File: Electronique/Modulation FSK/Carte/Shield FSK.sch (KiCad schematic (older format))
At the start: 13 parts, among them P1 CONN_1, U1 XR2206

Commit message: Et on reroute, on reroute, on reroute, on reroute, on reroute, on reroute, on reroute, on reroute, on reroute, on reroute, on reroute, on reroute, on reroute, on reroute, on reroute, on reroute, on reroute, on reroute, on reroute, on reroute, on reroute, on reroute, on reroute, on reroute, on reroute, on reroute, on reroute, on reroute, on reroute, on reroute, on reroute, on reroute, on reroute, on reroute, on reroute, on reroute, on reroute, on reroute, on reroute, on reroute, on reroute, on reroute, on reroute, on reroute. C'est fini !!!
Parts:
- removed C1, C4: CP, symbol CP
- removed P1: CONN_1, symbol CONN_1
- added C1, C4: C, symbol C
- added P1: BNC, symbol BNC
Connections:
- net GND: now also C1.2, C4.1, P1.2 (Ext)
- net at U1.10 (BIAS): now also C4.2
- net at U1.2 (STO): now also P1.1 (In)
- net at R1.2, R2.1, RV1.2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: now also C1.1
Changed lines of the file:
@@
-EESchema Schematic File Version 2  date 23/03/2012 16:19:35
+EESchema Schematic File Version 2  date 24/03/2012 16:53:15
 LIBS:power
 LIBS:device
@@
 LIBS:contrib
 LIBS:valves
-LIBS:Arduino
-LIBS:arduino_shieldsNCL
 LIBS:Shield FSK-cache
 EELAYER 25  0
@@
 Sheet 1 1
 Title ""
-Date "23 mar 2012"
+Date "24 mar 2012"
 Rev ""
 Comp ""
@@
 Comment4 ""
 $EndDescr
-$Comp
-L CONN_1 P1
-U 1 1 4F6C926A
+Wire Wire Line
+	6400 3000 6500 3000
+Wire Wire Line
+	4400 2100 4500 2100
+Wire Wire Line
+	2850 4200 2850 4000
+Wire Wire Line
+	2600 4550 2600 4650
+Wire Wire Line
+	2600 3650 2600 4050
+Connection ~ 2600 3850
+Wire Wire Line
+	3100 3850 3100 3700
+Wire Wire Line
+	3100 3700 4600 3700
+Wire Wire Line
+	6300 3800 6400 3800
+Wire Wire Line
+	6650 4000 6450 4000
+Wire Wire Line
+	6450 4000 6450 4100
+Wire Wire Line
+	6450 4100 6300 4100
+Connection ~ 3450 4350
+Wire Wire Line
+	3600 4350 3450 4350
+Wire Wire Line
+	4100 4350 4550 4350
+Wire Wire Line
+	4550 4350 4550 4200
+Wire Wire Line
+	4550 4200 4600 4200
+Wire Wire Line
+	4100 4150 4550 4150
+Wire Wire Line
+	4550 4150 4550 4100
+Wire Wire Line
+	4550 4100 4600 4100
+Wire Wire Line
+	4600 4000 4550 4000
+Wire Wire Line
+	4200 3850 4450 3850
+Connection ~ 4450 3800
+Wire Wire Line
+	4450 3850 4450 3800
+Wire Wire Line
+	6450 3900 6300 3900
+Wire Wire Line
+	4400 3800 4600 3800
+Wire Wire Line
+	4600 3500 4350 3500
+Wire Wire Line
+	3400 3600 4600 3600
+Wire Wire Line
+	3800 3850 3700 3850
+Wire Wire Line
+	4600 3900 4150 3900
+Wire Wire Line
+	4150 3900 4150 4000
+Wire Wire Line
+	3600 4150 3450 4150
+Wire Wire Line
+	3450 4150 3450 4500
+Wire Wire Line
+	6600 4200 6300 4200
+Wire Wire Line
+	7050 4000 7200 4000
+Wire Wire Line
+	6900 3800 6900 3700
+Wire Wire Line
+	6900 3700 6300 3700
+Wire Wire Line
+	2850 4000 2600 4000
+Connection ~ 2600 4000
+Wire Wire Line
+	2600 3050 2600 3150
+Wire Wire Line
+	2850 4600 2600 4600
+Connection ~ 2600 4600
+Wire Wire Line
+	4500 2200 4400 2200
+Wire Wire Line
+	3250 3300 3250 3400
+$Comp
+L GND #PWR3
+U 1 1 4F6DEC1B
+P 3250 3300
+F 0 "#PWR3" H 3250 3300 30  0001 C CNN
+F 1 "GND" H 3250 3230 30  0001 C CNN
+	1    3250 3300
+	-1   0    0    1
+$EndComp
+$Comp
+L BNC P1
+U 1 1 4F6DEBDE
 P 3250 3600
-F 0 "P1" H 3330 3600 40  0000 L CNN
-F 1 "CONN_1" H 3250 3655 30  0001 C CNN
+F 0 "P1" H 3260 3720 60  0000 C CNN
+F 1 "BNC" V 3360 3540 40  0000 C CNN
 	1    3250 3600
 	-1   0    0    1
 $EndComp
+$Comp
+L C C4
+U 1 1 4F6DEA2A
+P 6850 4000
+F 0 "C4" H 6900 4100 50  0000 L CNN
+F 1 "C" H 6900 3900 50  0000 L CNN
+	1    6850 4000
+	0    1    1    0
+$EndComp
+$Comp
+L C C1
+U 1 1 4F6DEA20
+P 2850 4400
+F 0 "C1" H 2900 4500 50  0000 L CNN
+F 1 "C" H 2900 4300 50  0000 L CNN
+	1    2850 4400
+	1    0    0    -1
+$EndComp
 Text Label 6500 3000 0    60   ~ 0
 Entree serie
-Wire Wire Line
-	6400 3000 6500 3000
-Wire Wire Line
-	4400 2100 4500 2100
-Wire Wire Line
-	2850 4200 2850 4000
-Wire Wire Line
-	2600 4550 2600 4650
-Wire Wire Line
-	2600 3650 2600 4050
-Connection ~ 2600 3850
-Wire Wire Line
-	3100 3850 3100 3700
-Wire Wire Line
-	3100 3700 4600 3700
-Wire Wire Line
-	6300 3800 6400 3800
-Wire Wire Line
-	6650 4000 6450 4000
-Wire Wire Line
-	6450 4000 6450 4100
-Wire Wire Line
-	6450 4100 6300 4100
-Connection ~ 3450 4350
-Wire Wire Line
-	3600 4350 3450 4350
-Wire Wire Line
-	4100 4350 4550 4350
-Wire Wire Line
-	4550 4350 4550 4200
-Wire Wire Line
-	4550 4200 4600 4200
-Wire Wire Line
-	4100 4150 4550 4150
-Wire Wire Line
-	4550 4150 4550 4100
-Wire Wire Line
-	4550 4100 4600 4100
-Wire Wire Line
-	4600 4000 4550 4000
-Wire Wire Line
-	4200 3850 4450 3850
-Connection ~ 4450 3800
-Wire Wire Line
-	4450 3850 4450 3800
-Wire Wire Line
-	6450 3900 6300 3900
-Wire Wire Line
-	4400 3800 4600 3800
-Wire Wire Line
-	4600 3500 4350 3500
-Wire Wire Line
-	3400 3600 4600 3600
-Wire Wire Line
-	3800 3850 3700 3850
-Wire Wire Line
-	4600 3900 4150 3900
-Wire Wire Line
-	4150 3900 4150 4000
-Wire Wire Line
-	3600 4150 3450 4150
-Wire Wire Line
-	3450 4150 3450 4500
-Wire Wire Line
-	6600 4200 6300 4200
-Wire Wire Line
-	7050 4000 7200 4000
-Wire Wire Line
-	6900 3800 6900 3700
-Wire Wire Line
-	6900 3700 6300 3700
-Wire Wire Line
-	2850 4000 2600 4000
-Connection ~ 2600 4000
-Wire Wire Line
-	2600 3050 2600 3150
-Wire Wire Line
-	2850 4600 2600 4600
-Connection ~ 2600 4600
-Wire Wire Line
-	4500 2200 4400 2200
-$Comp
-L GND #PWR7
+$Comp
+L GND #PWR8
 U 1 1 4F6B897D
 P 4400 2200
-F 0 "#PWR7" H 4400 2200 30  0001 C CNN
+F 0 "#PWR8" H 4400 2200 30  0001 C CNN
 F 1 "GND" H 4400 2130 30  0001 C CNN
 	1    4400 2200
@@
 $EndComp
 $Comp
-L +5V #PWR6
+L +5V #PWR7
 U 1 1 4F6B8971
 P 4400 2100
-F 0 "#PWR6" H 4400 2190 20  0001 C CNN
+F 0 "#PWR7" H 4400 2190 20  0001 C CNN
 F 1 "+5V" H 4400 2190 30  0000 C CNN
 	1    4400 2100
@@
 F 1 "ARDUINO_SHIELD" H 5500 1350 60  0000 C CNN
 	1    5450 2300
-	1    0    0    -1
-$EndComp
-$Comp
-L CP C4
-U 1 1 4F5B8873
-P 6850 4000
-F 0 "C4" H 6900 4100 50  0000 L CNN
-F 1 "CP" H 6900 3900 50  0000 L CNN
-	1    6850 4000
-	0    -1   -1   0
-$EndComp
-$Comp
-L CP C1
-U 1 1 4F5B87DA
-P 2850 4400
-F 0 "C1" H 2900 4500 50  0000 L CNN
-F 1 "CP" H 2900 4300 50  0000 L CNN
-	1    2850 4400
 	1    0    0    -1
 $EndComp
@@
 $EndComp
 $Comp
-L GND #PWR10
+L GND #PWR11
 U 1 1 4F5B75FB
 P 7200 4000
-F 0 "#PWR10" H 7200 4000 30  0001 C CNN
+F 0 "#PWR11" H 7200 4000 30  0001 C CNN
 F 1 "GND" H 7200 3930 30  0001 C CNN
 	1    7200 4000
@@
 Entree serie
 $Comp
-L GND #PWR3
+L GND #PWR4
 U 1 1 4F5B733F
 P 3450 4500
-F 0 "#PWR3" H 3450 4500 30  0001 C CNN
+F 0 "#PWR4" H 3450 4500 30  0001 C CNN
 F 1 "GND" H 3450 4430 30  0001 C CNN
 	1    3450 4500
@@
 $EndComp
 $Comp
-L GND #PWR4
+L GND #PWR5
 U 1 1 4F5B7223
 P 3700 3850
-F 0 "#PWR4" H 3700 3850 30  0001 C CNN
+F 0 "#PWR5" H 3700 3850 30  0001 C CNN
 F 1 "GND" H 3700 3780 30  0001 C CNN
 	1    3700 3850
@@
 $EndComp
 $Comp
-L GND #PWR5
+L GND #PWR6
 U 1 1 4F5B70E7
 P 4350 3500
-F 0 "#PWR5" H 4350 3500 30  0001 C CNN
+F 0 "#PWR6" H 4350 3500 30  0001 C CNN
 F 1 "GND" H 4350 3430 30  0001 C CNN
 	1    4350 3500
@@
 $EndComp
 $Comp
-L GND #PWR9
+L GND #PWR10
 U 1 1 4F5B7069
 P 6450 3900
-F 0 "#PWR9" H 6450 3900 30  0001 C CNN
+F 0 "#PWR10" H 6450 3900 30  0001 C CNN
 F 1 "GND" H 6450 3830 30  0001 C CNN
 	1    6450 3900
@@
 $EndComp
 $Comp
-L VCC #PWR8
+L VCC #PWR9
 U 1 1 4F5B7056
 P 4400 3800
-F 0 "#PWR8" H 4400 3900 30  0001 C CNN
+F 0 "#PWR9" H 4400 3900 30  0001 C CNN
 F 1 "VCC" H 4400 3900 30  0000 C CNN
 	1    4400 3800

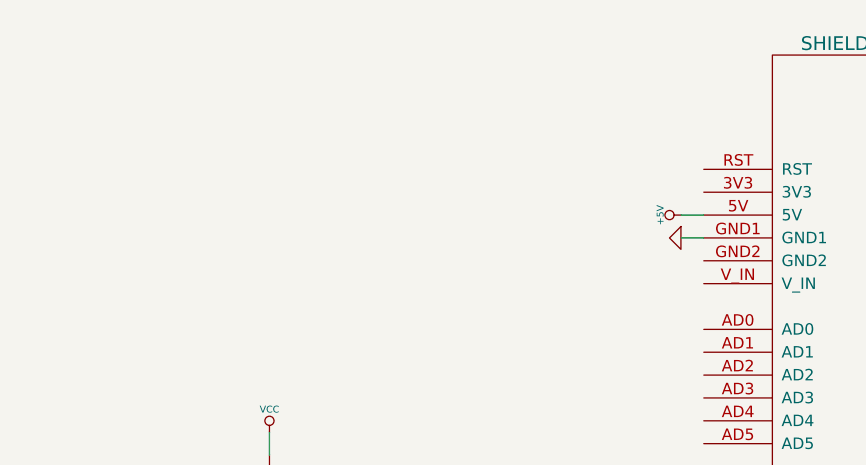
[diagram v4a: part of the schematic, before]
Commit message: Reroutage de la carte FSK, ajout d'un régulateur de tension spécifique et d'un bornier
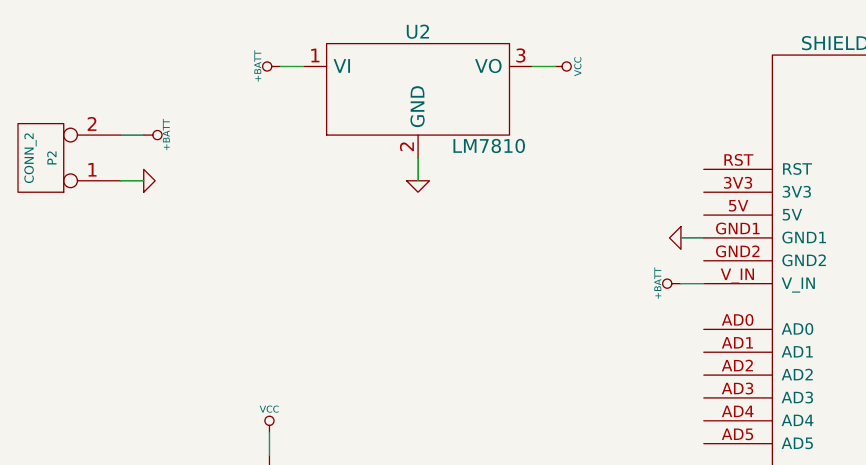
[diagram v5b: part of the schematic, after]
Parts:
- added P2: CONN_2, symbol CONN_2
- added U2: LM7810, symbol LM7810
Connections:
- net GND: now also P2.1 (P1), U2.2 (GND)
- net VCC: now also U2.3 (VO)
- net +BATT: now reaches SHIELD1.V_IN
- net +BATT: now also P2.2 (PM), U2.1 (VI)
- net +5V: no longer names the net of SHIELD1.5V
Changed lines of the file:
@@
-EESchema Schematic File Version 2  date 24/03/2012 16:53:15
+EESchema Schematic File Version 2  date 10/07/2012 11:17:02
 LIBS:power
 LIBS:device
@@
 LIBS:contrib
 LIBS:valves
+LIBS:Arduino
+LIBS:arduino_shieldsNCL
+LIBS:o_analog
 LIBS:Shield FSK-cache
 EELAYER 25  0
@@
 Sheet 1 1
 Title ""
-Date "24 mar 2012"
+Date "10 jul 2012"
 Rev ""
 Comp ""
@@
 $EndDescr
 Wire Wire Line
+	1950 1950 2050 1950
+Wire Wire Line
+	3250 1850 3250 1950
+Wire Wire Line
+	3850 1450 3750 1450
+Wire Wire Line
 	6400 3000 6500 3000
-Wire Wire Line
-	4400 2100 4500 2100
 Wire Wire Line
 	2850 4200 2850 4000
@@
 Wire Wire Line
 	3250 3300 3250 3400
-$Comp
-L GND #PWR3
+Wire Wire Line
+	4500 2400 4400 2400
+Wire Wire Line
+	2750 1450 2650 1450
+Wire Wire Line
+	1950 1750 2050 1750
+$Comp
+L GND #PWR01
+U 1 1 4FFBED7B
+P 2050 1950
+F 0 "#PWR01" H 2050 1950 30  0001 C CNN
+F 1 "GND" H 2050 1880 30  0001 C CNN
+	1    2050 1950
+	0    -1   -1   0
+$EndComp
+$Comp
+L +BATT #PWR02
+U 1 1 4FFBED73
+P 2050 1750
+F 0 "#PWR02" H 2050 1700 20  0001 C CNN
+F 1 "+BATT" H 2050 1850 30  0000 C CNN
+	1    2050 1750
+	0    1    1    0
+$EndComp
+$Comp
+L CONN_2 P2
+U 1 1 4FFBED61
+P 1600 1850
+F 0 "P2" V 1550 1850 40  0000 C CNN
+F 1 "CONN_2" V 1650 1850 40  0000 C CNN
+	1    1600 1850
+	-1   0    0    1
+$EndComp
+$Comp
+L +BATT #PWR03
+U 1 1 4FFBED15
+P 2650 1450
+F 0 "#PWR03" H 2650 1400 20  0001 C CNN
+F 1 "+BATT" H 2650 1550 30  0000 C CNN
+	1    2650 1450
+	0    -1   -1   0
+$EndComp
+$Comp
+L +BATT #PWR04
+U 1 1 4FFBED10
+P 4400 2400
+F 0 "#PWR04" H 4400 2350 20  0001 C CNN
+F 1 "+BATT" H 4400 2500 30  0000 C CNN
+	1    4400 2400
+	0    -1   -1   0
+$EndComp
+$Comp
+L VCC #PWR05
+U 1 1 4FFBE854
+P 3850 1450
+F 0 "#PWR05" H 3850 1550 30  0001 C CNN
+F 1 "VCC" H 3850 1550 30  0000 C CNN
+	1    3850 1450
+	0    1    1    0
+$EndComp
+$Comp
+L GND #PWR06
+U 1 1 4FFBE773
+P 3250 1950
+F 0 "#PWR06" H 3250 1950 30  0001 C CNN
+F 1 "GND" H 3250 1880 30  0001 C CNN
+	1    3250 1950
+	1    0    0    -1
+$EndComp
+$Comp
+L LM7810 U2
+U 1 1 4FFBE6BF
+P 3250 1550
+F 0 "U2" H 3250 1800 60  0000 C CNN
+F 1 "LM7810" H 3560 1300 60  0000 C CNN
+	1    3250 1550
+	1    0    0    -1
+$EndComp
+$Comp
+L GND #PWR07
 U 1 1 4F6DEC1B
 P 3250 3300
-F 0 "#PWR3" H 3250 3300 30  0001 C CNN
+F 0 "#PWR07" H 3250 3300 30  0001 C CNN
 F 1 "GND" H 3250 3230 30  0001 C CNN
 	1    3250 3300
@@
 Entree serie
 $Comp
-L GND #PWR8
+L GND #PWR08
 U 1 1 4F6B897D
 P 4400 2200
-F 0 "#PWR8" H 4400 2200 30  0001 C CNN
+F 0 "#PWR08" H 4400 2200 30  0001 C CNN
 F 1 "GND" H 4400 2130 30  0001 C CNN
 	1    4400 2200
 	0    1    1    0
-$EndComp
-$Comp
-L +5V #PWR7
-U 1 1 4F6B8971
-P 4400 2100
-F 0 "#PWR7" H 4400 2190 20  0001 C CNN
-F 1 "+5V" H 4400 2190 30  0000 C CNN
-	1    4400 2100
-	0    -1   -1   0
 $EndComp
 $Comp
@@
 $EndComp
 $Comp
-L GND #PWR2
+L GND #PWR09
 U 1 1 4F5B8724
 P 2600 4650
-F 0 "#PWR2" H 2600 4650 30  0001 C CNN
+F 0 "#PWR09" H 2600 4650 30  0001 C CNN
 F 1 "GND" H 2600 4580 30  0001 C CNN
 	1    2600 4650
@@
 $EndComp
 $Comp
-L VCC #PWR1
+L VCC #PWR010
 U 1 1 4F5B8719
 P 2600 3050
-F 0 "#PWR1" H 2600 3150 30  0001 C CNN
+F 0 "#PWR010" H 2600 3150 30  0001 C CNN
 F 1 "VCC" H 2600 3150 30  0000 C CNN
 	1    2600 3050
@@
 $EndComp
 $Comp
-L GND #PWR11
+L GND #PWR011
 U 1 1 4F5B75FB
 P 7200 4000
-F 0 "#PWR11" H 7200 4000 30  0001 C CNN
+F 0 "#PWR011" H 7200 4000 30  0001 C CNN
 F 1 "GND" H 7200 3930 30  0001 C CNN
 	1    7200 4000
@@
 Entree serie
 $Comp
-L GND #PWR4
+L GND #PWR012
 U 1 1 4F5B733F
 P 3450 4500
-F 0 "#PWR4" H 3450 4500 30  0001 C CNN
+F 0 "#PWR012" H 3450 4500 30  0001 C CNN
 F 1 "GND" H 3450 4430 30  0001 C CNN
 	1    3450 4500
@@
 $EndComp
 $Comp
-L GND #PWR5
+L GND #PWR013
 U 1 1 4F5B7223
 P 3700 3850
-F 0 "#PWR5" H 3700 3850 30  0001 C CNN
+F 0 "#PWR013" H 3700 3850 30  0001 C CNN
 F 1 "GND" H 3700 3780 30  0001 C CNN
 	1    3700 3850
@@
 $EndComp
 $Comp
-L GND #PWR6
+L GND #PWR014
 U 1 1 4F5B70E7
 P 4350 3500
-F 0 "#PWR6" H 4350 3500 30  0001 C CNN
+F 0 "#PWR014" H 4350 3500 30  0001 C CNN
 F 1 "GND" H 4350 3430 30  0001 C CNN
 	1    4350 3500
@@
 $EndComp
 $Comp
-L GND #PWR10
+L GND #PWR015
 U 1 1 4F5B7069
 P 6450 3900
-F 0 "#PWR10" H 6450 3900 30  0001 C CNN
+F 0 "#PWR015" H 6450 3900 30  0001 C CNN
 F 1 "GND" H 6450 3830 30  0001 C CNN
 	1    6450 3900
@@
 $EndComp
 $Comp
-L VCC #PWR9
+L VCC #PWR016
 U 1 1 4F5B7056
 P 4400 3800
-F 0 "#PWR9" H 4400 3900 30  0001 C CNN
+F 0 "#PWR016" H 4400 3900 30  0001 C CNN
 F 1 "VCC" H 4400 3900 30  0000 C CNN
 	1    4400 3800
